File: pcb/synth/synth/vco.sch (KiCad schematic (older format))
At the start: 49 parts

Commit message: analog synth updates
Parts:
- added C10, C11, C13, C14, C15, C16, C17, C7, C8, C9: 0.1u, Capacitor_SMD:C_0603_1608Metric_Pad1.05x0.95mm_HandSolder, symbol Device:C
- added C12, C18, C4: 1u, Capacitor_SMD:C_0603_1608Metric_Pad1.05x0.95mm_HandSolder, symbol Device:C
- added R24: 10k, Resistor_SMD:R_0603_1608Metric_Pad1.05x0.95mm_HandSolder, symbol Device:R_US
- added U7: OPA172IDBVR, Package_TO_SOT_SMD:SOT-23-5, symbol opa172idbvr:OPA172IDBVR
- C1, C2, C3, C5: renamed from C?; footprint (none) -> Capacitor_SMD:C_0603_1608Metric_Pad1.05x0.95mm_HandSolder
- C6: renamed from C?; value 680p -> 0.47u; footprint (none) -> Capacitor_SMD:C_0603_1608Metric_Pad1.05x0.95mm_HandSolder
- R1, R11, R12, R13, R14, R15, R16, R17, R18, R19, R2, R20, R21, R22, R23, R25, R26, R27, R28, R3, R4, R5, R6, R7, R8, R9: renamed from R?; footprint (none) -> Resistor_SMD:R_0603_1608Metric_Pad1.05x0.95mm_HandSolder
- R10: renamed from R?; value 20k -> 22; footprint (none) -> Resistor_SMD:R_0603_1608Metric_Pad1.05x0.95mm_HandSolder
- R29: renamed from R?; value 20K -> 100k; footprint (none) -> Resistor_SMD:R_0603_1608Metric_Pad1.05x0.95mm_HandSolder
- U1, U2, U3: renamed from U?; footprint (none) -> Package_SO:SOIC-16_3.9x9.9mm_P1.27mm
- gave numbers to parts that had none: 1
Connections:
- net +12V: now also R28.1, C10.1, C11.1, C12.1, C7.1, C8.1, C9.1, U7.5 (V+)
- net -12V: now also C13.2, C14.2, C15.2, C16.2, C17.2, C18.2, U7.2 (V-)
- net AN_SQR: now also U7.1, U7.4 (-); no longer C5.2
- net CTRL_VCO: no longer R28.1
- net GND: now also C10.2, C11.2, C12.2, C13.1, C14.1, C15.1, C16.1, C17.1, C18.1, C7.2, C8.2, C9.2, R24.1
- net at R26.1, U6.1: now also C4.1; no longer R22.2, U3.4 (-)
- net at C6.1, U3.10, U3.12: now also R24.2
- new net: C5.2, U7.3 (+)
- new net: C4.2, R22.2, U3.4 (-)
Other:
- note removed: "TO DO:\n- verify schematic and component values against breadboard\n- add decoupling"
- moved on the sheet: C5, C6, R21, R22, R23, R25, R26, R27, R28, R29, U3A, U3B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

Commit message: final pcb designs and initial i2c
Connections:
- no-connect marks 1 -> 7
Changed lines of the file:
@@
 Wire Wire Line
 	3950 6900 3950 7050
+NoConn ~ 6250 2850
+NoConn ~ 8300 2850
+NoConn ~ 2450 2850
+NoConn ~ 3900 2850
+NoConn ~ 4550 4900
+NoConn ~ 7950 5000
 $EndSCHEMATC

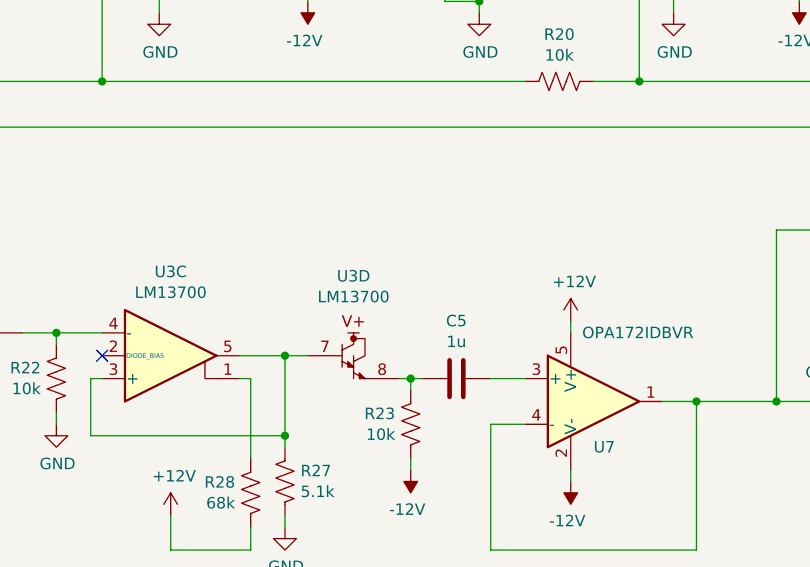
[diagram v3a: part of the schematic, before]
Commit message: implemented 2 wiproc design with one streaming to other and printing to terminal
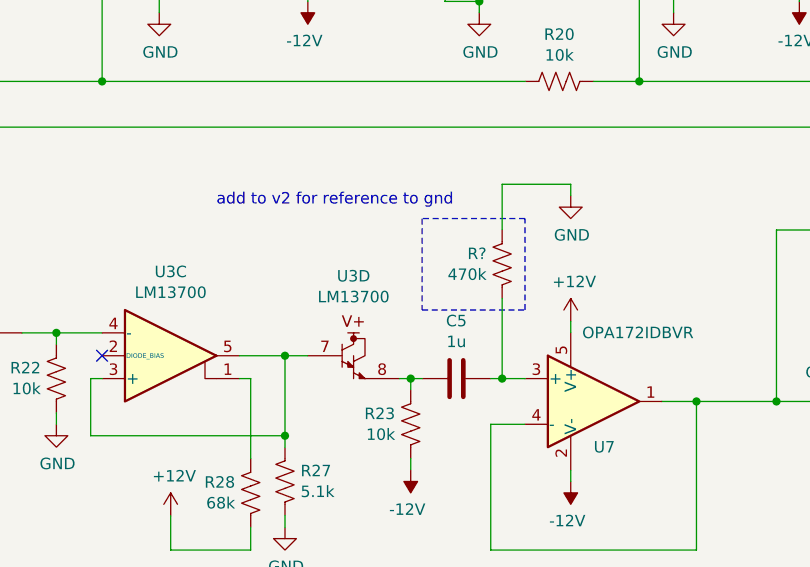
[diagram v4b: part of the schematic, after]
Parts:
- added R?: 470k, Resistor_SMD:R_0603_1608Metric_Pad1.05x0.95mm_HandSolder, symbol Device:R_US
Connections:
- net GND: now also R?.2
- net at C5.2, U7.3 (+): now also R?.1
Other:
- note added: "add to v2 for reference to gnd"
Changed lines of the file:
@@
 	6600 4800 6600 4750
 Wire Wire Line
-	6250 5000 6400 5000
+	6250 5000 6300 5000
 Wire Wire Line
 	6250 5200 6250 5750
@@
 NoConn ~ 4550 4900
 NoConn ~ 7950 5000
+$Comp
+L Device:R_US R?
+U 1 1 5DE4EB04
+P 6300 4500
+F 0 "R?" H 6232 4454 50  0000 R CNN
+F 1 "470k" H 6232 4545 50  0000 R CNN
+F 2 "Resistor_SMD:R_0603_1608Metric_Pad1.05x0.95mm_HandSolder" V 6340 4490 50  0001 C CNN
+F 3 "~" H 6300 4500 50  0001 C CNN
+	1    6300 4500
+	1    0    0    1
+$EndComp
+Wire Wire Line
+	6300 4650 6300 5000
+Connection ~ 6300 5000
+Wire Wire Line
+	6300 5000 6400 5000
+$Comp
+L power:GND #PWR?
+U 1 1 5DE6E779
+P 6600 4200
+F 0 "#PWR?" H 6600 3950 50  0001 C CNN
+F 1 "GND" H 6605 4027 50  0000 C CNN
+F 2 "" H 6600 4200 50  0001 C CNN
+F 3 "" H 6600 4200 50  0001 C CNN
+	1    6600 4200
+	1    0    0    -1
+$EndComp
+Wire Wire Line
+	6600 4200 6600 4150
+Wire Wire Line
+	6600 4150 6300 4150
+Wire Wire Line
+	6300 4150 6300 4350
+Wire Notes Line
+	6400 4300 5950 4300
+Wire Notes Line
+	5950 4300 5950 4700
+Wire Notes Line
+	5950 4700 6400 4700
+Wire Notes Line
+	6400 4700 6400 4300
+Text Notes 5050 4250 0    50   ~ 0
+add to v2 for reference to gnd
 $EndSCHEMATC
